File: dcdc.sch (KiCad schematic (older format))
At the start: 41 parts

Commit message: Minor schematic update
Signed-off-by: Patrick Rudolph <siro@das-labor.org>
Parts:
- added C?: 100n, symbol Device:C_Small
- added C? (x2): ?, symbol Device:C_Small
- added Q?: BSS123, Package_DirectFET:DirectFET_MN, symbol Transistor_FET:IRF6668
- added R?: ?, symbol Device:R
- added R?: 20k, symbol Device:R
- added R?: 158k, symbol Device:R
- C?: value C_Small -> 100p
- R?: value R -> 33
- U?: value MAX5069 -> MAX5069D
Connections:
- net GND: now also U?.2 (SYNC), C?.2, C?.2, C?.2, Q?.3 (S), R?.1, R?.2
- net SHUTDOWN: now also Q?.2 (G)
- net at U?.3 (SCOMP): now also C?.1
- net at U?.5 (UVLO): now also Q?.1 (D), R?.1, R?.2
- net at U?.7 (COMP): now also C?.1, R?.1
- net at U?.8 (FLTINT): now also C?.1
- net V_12V renamed +12V
- net +12V: now also R?.2
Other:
- note added: "50ns deadtime"
- note added: "5Mhz cutoff"
- note added: "Vstart = 11V"
- note added: "fault integration time 4.7ms"
- note added: "fosc = 600Khz"
- note added: "pull low to disable MAX5069D"
- moved on the sheet: R?

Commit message: Huge schematic and documentation update
Signed-off-by: Patrick Rudolph <siro@das-labor.org>
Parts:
- added C?: 100n, symbol Device:C_Small
- added C?: 1u, symbol Device:C_Small
- added U?: MCP4725, symbol MICROCHIP:MCP4725
- added U?: LDK320AU50R, Package_TO_SOT_SMD:SOT-89-3, symbol Regulator_Linear:L78L05_SOT89
- L?: value 22u -> 300u; footprint (none) -> Inductor_THT:L_Toroid_Vertical_L21.6mm_W9.1mm_P8.40mm_Bourns_5700
- R?: value 19k -> 10k
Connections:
- net 12V+_isolated: now also U?.3 (IN); no longer R?.2
- net 3.3V: now also C?.1, U?.3 (Vdd)
- net GND: now also C?.2, U?.2 (Vss), U?.6 (A0)
- net GNDA: now also C?.2, U?.2 (GND)
- net DAC_Ilimit renamed DAC
- net DAC: now also U?.1 (Vout)
- new net +5VA: C?.1, R?.2, U?.1 (OUT)
- new net SCL: U?.5 (SCL)
- new net SDA: U?.4 (SDA)
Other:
- note added: "3.3V - 1.5V\n"
- note added: "Adjustable current limit"
- note added: "SiC 5A"
- note added: "TBD"
- note added: "Vin nominal 30 - 50V\nAin = 9.33A - 14A @ 50V\nAin = 12A @ 30V\n-----------\nVout = 240V\nAout = 1.4A (+- 0.25A)"
- note added: "address: 1100000"
- note added: "couple thermal"
- note removed: "3.3V - 2.1V\n"
- moved on the sheet: C?, R?

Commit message: Add more packages
Signed-off-by: Patrick Rudolph <siro@das-labor.org>
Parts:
- C? (x2): footprint (none) -> Capacitor_SMD:C_0603_1608Metric
- C? (x2): footprint (none) -> Capacitor_SMD:C_1206_3216Metric
- C?: footprint (none) -> Capacitor_SMD:C_0805_2012Metric
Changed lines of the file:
@@
 EESchema Schematic File Version 4
 LIBS:mppt_power-cache
-EELAYER 29 0
+EELAYER 30 0
 EELAYER END
 $Descr A4 11693 8268
@@
 F 0 "C?" H 4292 2946 50  0000 L CNN
 F 1 "100p" H 4292 2855 50  0000 L CNN
-F 2 "" H 4200 2900 50  0001 C CNN
+F 2 "Capacitor_SMD:C_0603_1608Metric" H 4200 2900 50  0001 C CNN
 F 3 "~" H 4200 2900 50  0001 C CNN
 	1    4200 2900
@@
 F 0 "C?" H 6442 1896 50  0000 L CNN
 F 1 "1u" H 6442 1805 50  0000 L CNN
-F 2 "" H 6350 1850 50  0001 C CNN
+F 2 "Capacitor_SMD:C_1206_3216Metric" H 6350 1850 50  0001 C CNN
 F 3 "~" H 6350 1850 50  0001 C CNN
 	1    6350 1850
@@
 F 0 "C?" H 6142 1896 50  0000 L CNN
 F 1 "1u" H 6142 1805 50  0000 L CNN
-F 2 "" H 6050 1850 50  0001 C CNN
+F 2 "Capacitor_SMD:C_1206_3216Metric" H 6050 1850 50  0001 C CNN
 F 3 "~" H 6050 1850 50  0001 C CNN
 	1    6050 1850
@@
 F 0 "C?" H 3992 1996 50  0000 L CNN
 F 1 "100n" H 3992 1905 50  0000 L CNN
-F 2 "" H 3900 1950 50  0001 C CNN
+F 2 "Capacitor_SMD:C_0603_1608Metric" H 3900 1950 50  0001 C CNN
 F 3 "~" H 3900 1950 50  0001 C CNN
 	1    3900 1950
@@
 F 0 "C?" H 3992 2346 50  0000 L CNN
 F 1 "1u" H 3992 2255 50  0000 L CNN
-F 2 "" H 3900 2300 50  0001 C CNN
+F 2 "Capacitor_SMD:C_0805_2012Metric" H 3900 2300 50  0001 C CNN
 F 3 "~" H 3900 2300 50  0001 C CNN
 	1    3900 2300

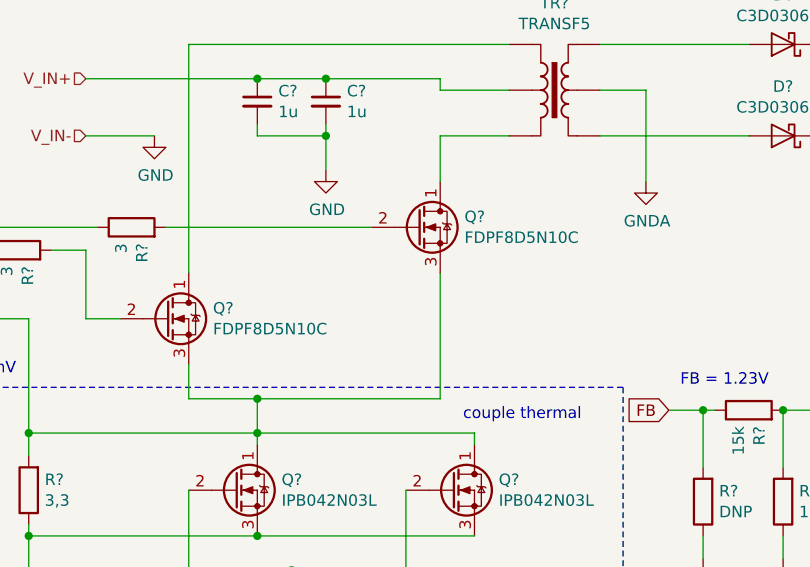
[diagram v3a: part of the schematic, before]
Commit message: Switch FET to SMD
Signed-off-by: Patrick Rudolph <siro@das-labor.org>
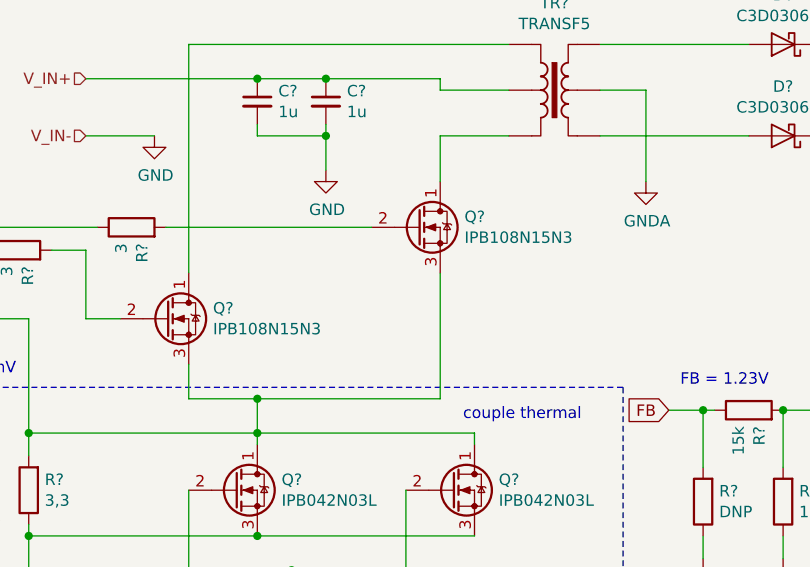
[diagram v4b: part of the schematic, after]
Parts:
- Q? (x2): value FDPF8D5N10C -> IPB108N15N3; footprint Package_DirectFET:DirectFET_MN -> Package_TO_SOT_SMD:TO-263-2
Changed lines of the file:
@@
 P 5650 2800
 F 0 "Q?" H 5856 2846 50  0000 L CNN
-F 1 "FDPF8D5N10C" H 5856 2755 50  0000 L CNN
-F 2 "Package_DirectFET:DirectFET_MN" H 5650 2800 50  0001 C CIN
+F 1 "IPB108N15N3" H 5856 2755 50  0000 L CNN
+F 2 "Package_TO_SOT_SMD:TO-263-2" H 5650 2800 50  0001 C CIN
 F 3 "https://www.mouser.de/datasheet/2/308/FDP8D5N10C-D-1315649.pdf" H 5650 2800 50  0001 L CNN
 	1    5650 2800
@@
 AR Path="/5D82C26D/5D834AF5" Ref="Q?"  Part="1"
 F 0 "Q?" H 6956 2446 50  0000 L CNN
-F 1 "FDPF8D5N10C" H 6956 2355 50  0000 L CNN
-F 2 "Package_DirectFET:DirectFET_MN" H 6750 2400 50  0001 C CIN
+F 1 "IPB108N15N3" H 6956 2355 50  0000 L CNN
+F 2 "Package_TO_SOT_SMD:TO-263-2" H 6750 2400 50  0001 C CIN
 F 3 "https://www.mouser.de/datasheet/2/308/FDP8D5N10C-D-1315649.pdf" H 6750 2400 50  0001 L CNN
 	1    6750 2400

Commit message: Split into more schematics, add more comments
Signed-off-by: Patrick Rudolph <siro@das-labor.org>
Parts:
- removed R?: 1k, symbol Device:R
- added C? (x14): 10u, Capacitor_SMD:C_1206_3216Metric, symbol Device:C_Small
- added C?: 100n, symbol Device:C_Small
- added J? (x2): Screw_Terminal_01x02, symbol Connector:Screw_Terminal_01x02
- added R?: 10k, symbol Device:R
- added TP? (x3): TestPoint, symbol Connector:TestPoint
- C? (x2): value 22u -> 10u
- R? (x2): value 1k -> 100k
- R?: value 1k -> 640
- R?: value 15k -> 150k
- U?: value SFH617A-2 -> SFH617A-1X007T
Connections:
- net +5VA: now also C?.1, TP?.1
- net DAC: now also TP?.1
- net GND: now also C?.2, C?.2, C?.2, C?.2, C?.2, C?.2, C?.2, C?.2, C?.2, C?.2, C?.2, C?.2, J?.2 (Pin_2), R?.1
- net GNDA: now also C?.2, C?.2, C?.2
- net V_IN+: now also J?.1 (Pin_1); no longer C?.1, C?.1, TR?.2
- net V_OUT+: now also C?.1, C?.1
- net at Q?.1 (D), R?.1, R?.2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: now also TP?.1
- net at R?.2, R?.2, U?.3: now also R?.2
- new net: C?.1, C?.1, C?.1, C?.1, C?.1, C?.1, C?.1, C?.1, C?.1, C?.1, C?.1, C?.1, C?.1, C?.1, J?.1 (Pin_1), J?.2 (Pin_2), TR?.2
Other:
- note added: "C=1/(2*pi*fz*R)"
- note added: "CTF: 40%-80% @ 10mA"
- note added: "G1= 0.316 / 22 = 0,0144"
- note added: "G2 = Rpullup * CTR / Rled = 10k * 0,4 / 180 = 22"
- note added: "Input ripple should be less than 75 mV\nAdd 125uF ceramic at least"
- note added: "R = G1 * R1 * SQRT(1+(fc/fp)^2)/SQRT(1+(fz/fc)^2) ="
- note added: "Rledmax <=(Rpullup CTRmin) (Vsupply - Vf - Vtl431)/\n(Vdd - Vce,sat + Ibias CTRmin Rpullup) \n= (10k * 0,4) (5 - 1.1 - 1.24) /( 10.8 - 0,3 + 0.001 * 0,4 * 10k) =733\n"
- note added: "bias TL431 at 1mA -> Rbias = Vf / 1mA = 1k"
- note added: "depends on filter response"
- note added: "for debugging only"
- note removed: "FIXME: gain"
- moved on the sheet: C?, Q?, R?, U?
